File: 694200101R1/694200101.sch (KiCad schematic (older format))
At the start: 241 parts, among them J1 USB4085-GF-A, J2 Conn_01x02_Male, J3 Conn_01x02_Male, SW1 MX_SW, SW10 MX_SW, SW100 MX_SW, SW101 MX_SW, SW102 MX_SW, SW103 MX_SW, SW104 MX_SW, SW105 MX_SW, SW106 MX_SW, SW107 MX_SW, SW11 MX_SW, SW12 MX_SW, SW13 MX_SW, SW14 MX_SW, SW15 MX_SW, SW16 MX_SW, SW17 MX_SW, SW18 MX_SW, SW19 MX_SW, SW2 MX_SW, SW20 MX_SW, SW21 MX_SW, SW22 MX_SW, SW23 MX_SW, SW24 MX_SW, SW25 MX_SW, SW26 MX_SW, SW27 MX_SW, SW28 MX_SW, SW29 MX_SW, SW3 MX_SW, SW30 MX_SW, SW31 MX_SW, SW32 MX_SW, SW33 MX_SW, SW34 MX_SW, SW35 MX_SW, SW36 MX_SW, SW37 MX_SW, SW38 MX_SW, SW39 MX_SW, SW4 MX_SW, SW40 MX_SW, SW41 MX_SW, SW42 MX_SW, SW43 MX_SW, SW44 MX_SW, SW45 MX_SW, SW46 MX_SW, SW47 MX_SW, SW48 MX_SW, SW49 MX_SW, SW5 MX_SW, SW50 MX_SW, SW51 MX_SW, SW52 MX_SW, SW53 MX_SW, SW54 MX_SW, SW55 MX_SW, SW56 MX_SW, SW57 MX_SW, SW58 MX_SW, SW59 MX_SW, SW6 MX_SW, SW60 MX_SW, SW61 MX_SW, SW62 MX_SW, SW63 MX_SW, SW64 MX_SW, SW65 MX_SW, SW66 MX_SW, SW67 MX_SW, SW68 MX_SW, SW69 MX_SW, SW7 MX_SW, SW70 MX_SW, SW71 MX_SW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

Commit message: Added New Crystal to Schematic
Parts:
- removed Y1: Crystal_GND24, symbol Device:Crystal_GND24
- added Y?: ECS-480-10-33B-CKM-TR, cldg:XTAL_ECS-480-10-33B-CKM-TR, symbol cldg:ECS-480-10-33B-CKM-TR
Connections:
- wire segments 629 -> 623
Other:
- moved on the sheet: C4, C6

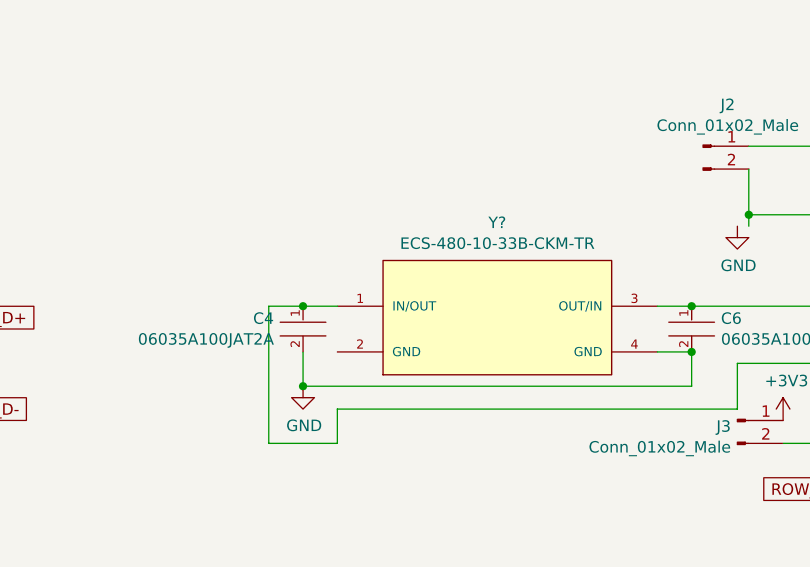
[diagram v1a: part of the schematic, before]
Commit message: LED rows 2+3
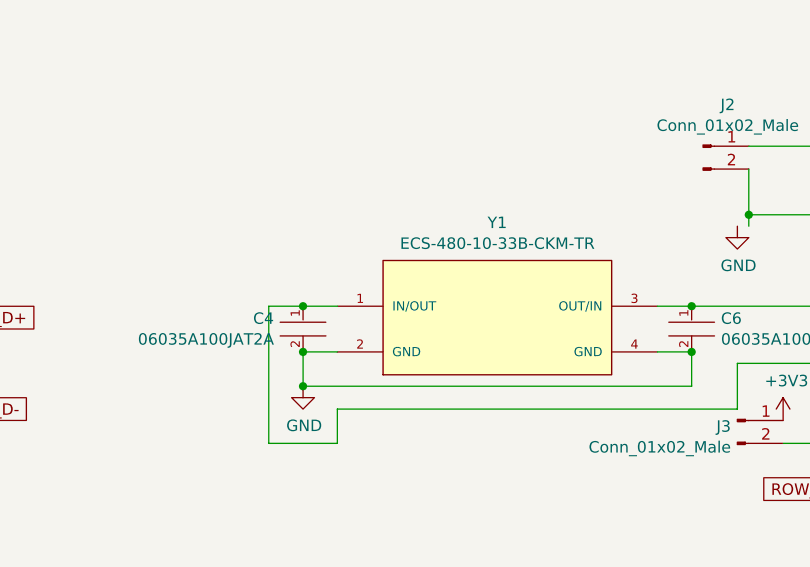
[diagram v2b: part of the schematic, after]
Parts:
- gave numbers to parts that had none: 1
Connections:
- net GND: now also Y1.2 (GND)
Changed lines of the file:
@@
 	7150 7500 7300 7500
 $Comp
-L cldg:ECS-480-10-33B-CKM-TR Y?
+L cldg:ECS-480-10-33B-CKM-TR Y1
 U 1 1 5FF4EA01
 P 6450 7400
-F 0 "Y?" H 6450 7865 50  0000 C CNN
+F 0 "Y1" H 6450 7865 50  0000 C CNN
 F 1 "ECS-480-10-33B-CKM-TR" H 6450 7774 50  0000 C CNN
 F 2 "cldg:XTAL_ECS-480-10-33B-CKM-TR" H 6150 7750 50  0001 L BNN
@@
 	7900 7300 7300 7300
 Connection ~ 7300 7300
+Wire Wire Line
+	5750 7500 5600 7500
+Connection ~ 5600 7500
 $EndSCHEMATC

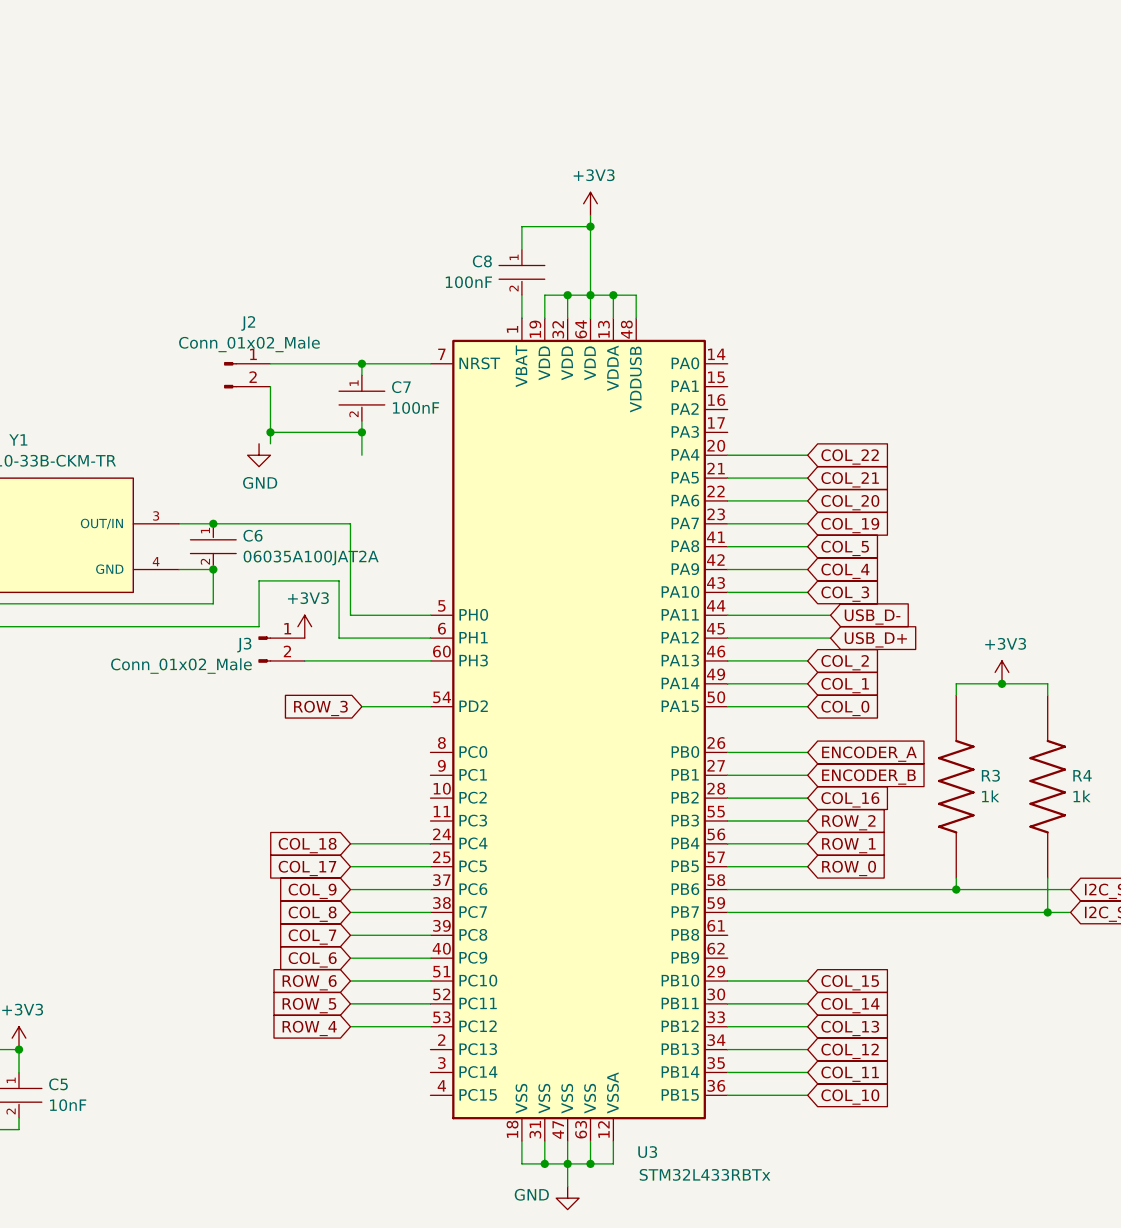
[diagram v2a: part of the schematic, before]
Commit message: Added Debug Header for Nucleo
Added debug headers for ST-V2-1 Nucleo board for advanced debugging
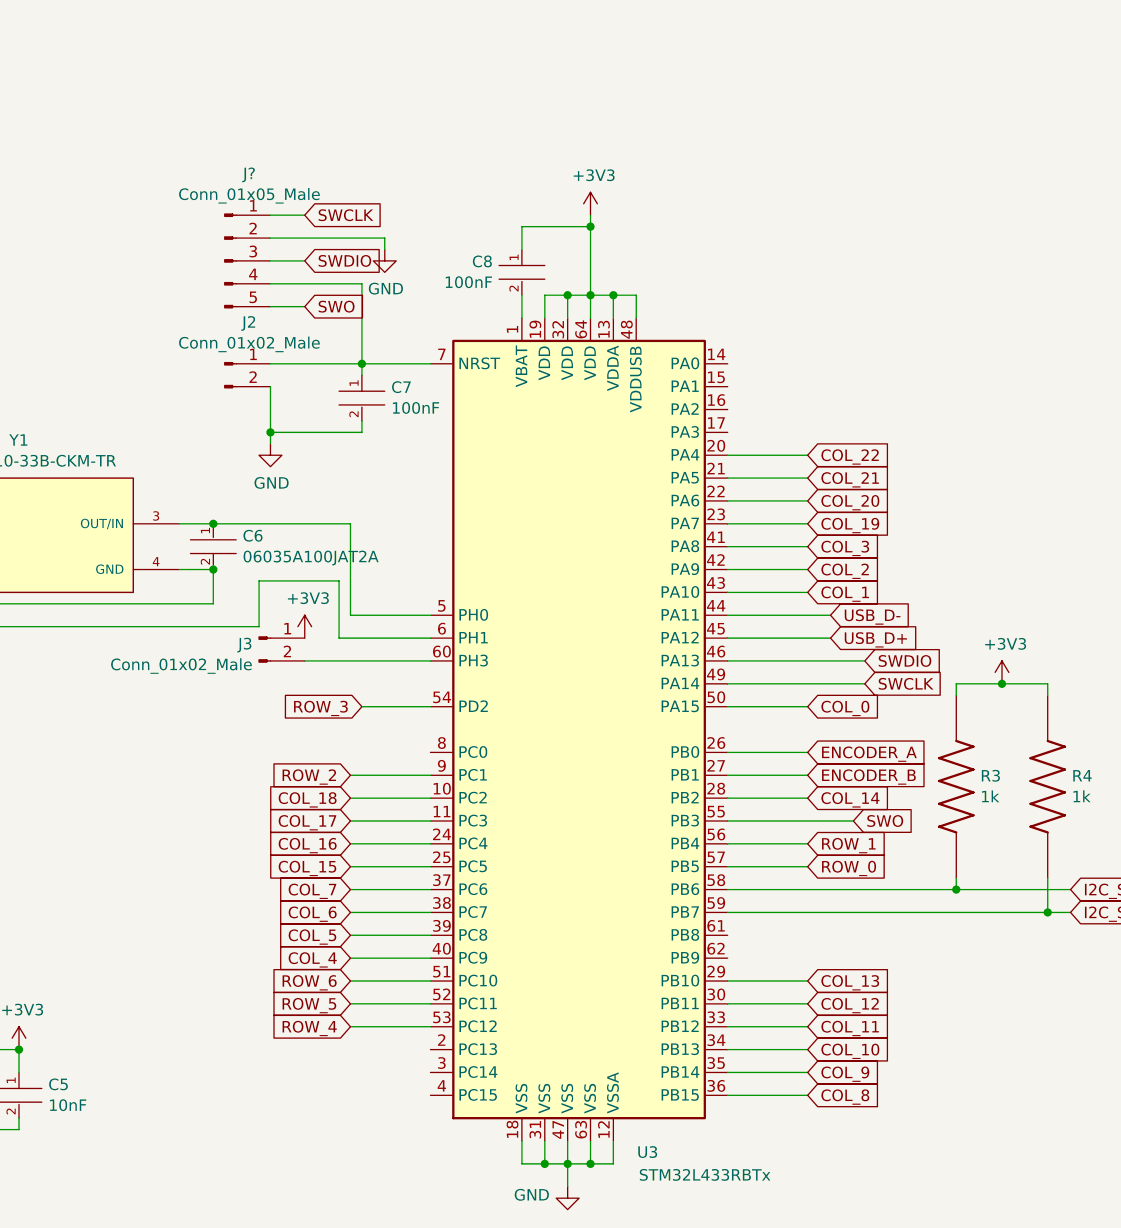
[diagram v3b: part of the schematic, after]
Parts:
- added J?: Conn_01x05_Male, Connector_PinHeader_2.54mm:PinHeader_1x05_P2.54mm_Vertical, symbol Connector:Conn_01x05_Male
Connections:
- net COL_1: now also U3.43 (PA10); no longer U3.49 (PA14)
- net COL_10: now also U3.34 (PB13); no longer U3.36 (PB15)
- net COL_11: now also U3.33 (PB12); no longer U3.35 (PB14)
- net COL_12: now also U3.30 (PB11); no longer U3.34 (PB13)
- net COL_13: now also U3.29 (PB10); no longer U3.33 (PB12)
- net COL_14: now also U3.28 (PB2); no longer U3.30 (PB11)
- net COL_15: now also U3.25 (PC5); no longer U3.29 (PB10)
- net COL_16: now also U3.24 (PC4); no longer U3.28 (PB2)
- net COL_17: now also U3.11 (PC3); no longer U3.25 (PC5)
- net COL_18: now also U3.10 (PC2); no longer U3.24 (PC4)
- net COL_2: now also U3.42 (PA9); no longer U3.46 (PA13)
- net COL_3: now also U3.41 (PA8); no longer U3.43 (PA10)
- net COL_4: now also U3.40 (PC9); no longer U3.42 (PA9)
- net COL_5: now also U3.39 (PC8); no longer U3.41 (PA8)
- net COL_6: now also U3.38 (PC7); no longer U3.40 (PC9)
- net COL_7: now also U3.37 (PC6); no longer U3.39 (PC8)
- net COL_8: now also U3.36 (PB15); no longer U3.38 (PC7)
- net COL_9: now also U3.35 (PB14); no longer U3.37 (PC6)
- net GND: now also C7.2, J2.2 (Pin_2), J?.2 (Pin_2)
- net ROW_2: now also U3.9 (PC1); no longer U3.55 (PB3)
- net at C7.1, J2.1 (Pin_1), U3.7 (NRST): now also J?.4 (Pin_4)
- new net SWCLK: J?.1 (Pin_1), U3.49 (PA14)
- new net SWDIO: J?.3 (Pin_3), U3.46 (PA13)
- new net SWO: J?.5 (Pin_5), U3.55 (PB3)
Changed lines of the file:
@@
 L power:GND #PWR09
 U 1 1 6007927B
-P 7500 6950
-F 0 "#PWR09" H 7500 6700 50  0001 C CNN
-F 1 "GND" H 7505 6777 50  0000 C CNN
-F 2 "" H 7500 6950 50  0001 C CNN
-F 3 "" H 7500 6950 50  0001 C CNN
-	1    7500 6950
+P 7550 6950
+F 0 "#PWR09" H 7550 6700 50  0001 C CNN
+F 1 "GND" H 7555 6777 50  0000 C CNN
+F 2 "" H 7550 6950 50  0001 C CNN
+F 3 "" H 7550 6950 50  0001 C CNN
+	1    7550 6950
 	1    0    0    -1
 $EndComp
@@
 Text GLabel 9900 8700 2    50   Input ~ 0
 ROW_1
-Text GLabel 9900 8600 2    50   Input ~ 0
+Text GLabel 7900 8400 0    50   Input ~ 0
 ROW_2
 Wire Wire Line
@@
 Text GLabel 9900 8100 2    50   Input ~ 0
 COL_0
-Text GLabel 9900 8000 2    50   Input ~ 0
+Text GLabel 9900 7600 2    50   Input ~ 0
 COL_1
-Text GLabel 9900 7900 2    50   Input ~ 0
+Text GLabel 9900 7500 2    50   Input ~ 0
 COL_2
-Text GLabel 9900 7600 2    50   Input ~ 0
+Text GLabel 9900 7400 2    50   Input ~ 0
 COL_3
-Text GLabel 9900 7500 2    50   Input ~ 0
+Text GLabel 7900 9200 0    50   Input ~ 0
 COL_4
-Text GLabel 9900 7400 2    50   Input ~ 0
+Text GLabel 7900 9100 0    50   Input ~ 0
 COL_5
 Wire Wire Line
 	8250 9200 7900 9200
-Text GLabel 7900 9200 0    50   Input ~ 0
+Text GLabel 7900 9000 0    50   Input ~ 0
 COL_6
 Wire Wire Line
 	8250 9100 7900 9100
-Text GLabel 7900 9100 0    50   Input ~ 0
+Text GLabel 7900 8900 0    50   Input ~ 0
 COL_7
 Wire Wire Line
 	8250 9000 7900 9000
-Text GLabel 7900 9000 0    50   Input ~ 0
+Text GLabel 9900 9800 2    50   Input ~ 0
 COL_8
 Wire Wire Line
 	8250 8900 7900 8900
-Text GLabel 7900 8900 0    50   Input ~ 0
+Text GLabel 9900 9700 2    50   Input ~ 0
 COL_9
-Text GLabel 9900 9800 2    50   Input ~ 0
+Text GLabel 9900 9600 2    50   Input ~ 0
 COL_10
-Text GLabel 9900 9700 2    50   Input ~ 0
+Text GLabel 9900 9500 2    50   Input ~ 0
 COL_11
-Text GLabel 9900 9600 2    50   Input ~ 0
+Text GLabel 9900 9400 2    50   Input ~ 0
 COL_12
-Text GLabel 9900 9500 2    50   Input ~ 0
+Text GLabel 9900 9300 2    50   Input ~ 0
 COL_13
-Text GLabel 9900 9400 2    50   Input ~ 0
+Text GLabel 9900 8500 2    50   Input ~ 0
 COL_14
-Text GLabel 9900 9300 2    50   Input ~ 0
+Text GLabel 7900 8800 0    50   Input ~ 0
 COL_15
-Text GLabel 9900 8500 2    50   Input ~ 0
+Text GLabel 7900 8700 0    50   Input ~ 0
 COL_16
 Wire Wire Line
 	8250 8800 7900 8800
-Text GLabel 7900 8800 0    50   Input ~ 0
+Text GLabel 7900 8600 0    50   Input ~ 0
 COL_17
 Wire Wire Line
 	8250 8700 7900 8700
-Text GLabel 7900 8700 0    50   Input ~ 0
+Text GLabel 7900 8500 0    50   Input ~ 0
 COL_18
 Text GLabel 9900 7300 2    50   Input ~ 0
@@
 	9550 8700 9900 8700
 Wire Wire Line
-	9550 8600 9900 8600
-Wire Wire Line
 	9550 8500 9900 8500
 Wire Wire Line
@@
 	9550 8100 9900 8100
 Wire Wire Line
-	9550 8000 9900 8000
+	9550 8000 10150 8000
 Wire Wire Line
-	9550 7900 9900 7900
+	9550 7900 10150 7900
 Wire Wire Line
 	10000 7800 9550 7800
@@
 Wire Wire Line
 	9550 7600 9900 7600
-Wire Wire Line
-	7950 7000 7950 6900
-Connection ~ 7950 6900
 $Comp
 L MCU_ST_STM32L4:STM32L433RBTx U3
@@
 	5750 7500 5600 7500
 Connection ~ 5600 7500
+Wire Wire Line
+	8250 8600 7900 8600
+Wire Wire Line
+	8250 8500 7900 8500
+Text GLabel 10150 7900 2    50   Input ~ 0
+SWDIO
+Text GLabel 10150 8000 2    50   Input ~ 0
+SWCLK
+$Comp
+L Connector:Conn_01x05_Male J?
+U 1 1 600F5E13
+P 7350 6150
+F 0 "J?" H 7458 6531 50  0000 C CNN
+F 1 "Conn_01x05_Male" H 7458 6440 50  0000 C CNN
+F 2 "Connector_PinHeader_2.54mm:PinHeader_1x05_P2.54mm_Vertical" H 7350 6150 50  0001 C CNN
+F 3 "~" H 7350 6150 50  0001 C CNN
+	1    7350 6150
+	1    0    0    -1
+$EndComp
+Wire Wire Line
+	8250 8400 7900 8400
+Text GLabel 10100 8600 2    50   Input ~ 0
+SWO
+Wire Wire Line
+	9550 8600 10100 8600
+Wire Wire Line
+	7550 5950 7700 5950
+Text GLabel 7700 5950 2    50   Input ~ 0
+SWCLK
+Wire Wire Line
+	7550 6050 8050 6050
+Wire Wire Line
+	8050 6050 8050 6100
+$Comp
+L power:GND #PWR?
+U 1 1 602A2E5A
+P 8050 6100
+F 0 "#PWR?" H 8050 5850 50  0001 C CNN
+F 1 "GND" H 8055 5927 50  0000 C CNN
+F 2 "" H 8050 6100 50  0001 C CNN
+F 3 "" H 8050 6100 50  0001 C CNN
+	1    8050 6100
+	1    0    0    -1
+$EndComp
+Wire Wire Line
+	7550 6150 7700 6150
+Text GLabel 7700 6150 2    50   Input ~ 0
+SWDIO
+Wire Wire Line
+	7950 6600 7950 6250
+Wire Wire Line
+	7950 6250 7550 6250
+Wire Wire Line
+	7550 6350 7700 6350
+Text GLabel 7700 6350 2    50   Input ~ 0
+SWO
 $EndSCHEMATC

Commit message: updated j2
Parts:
- removed J2: Conn_01x02_Male, Connector_PinHeader_2.54mm:PinHeader_1x02_P2.54mm_Vertical, symbol Connector:Conn_01x02_Male
- gave numbers to parts that had none: 1
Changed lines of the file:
@@
 	8850 10100 8850 10200
 $Comp
-L Connector:Conn_01x02_Male J2
-U 1 1 6006794B
-P 7350 6600
-F 0 "J2" H 7458 6781 50  0000 C CNN
-F 1 "Conn_01x02_Male" H 7458 6690 50  0000 C CNN
-F 2 "Connector_PinHeader_2.54mm:PinHeader_1x02_P2.54mm_Vertical" H 7350 6600 50  0001 C CNN
-F 3 "~" H 7350 6600 50  0001 C CNN
-	1    7350 6600
-	1    0    0    -1
-$EndComp
-$Comp
 L Connector:Conn_01x02_Male J3
 U 1 1 6006B89E
@@
 L power:GND #PWR09
 U 1 1 6007927B
-P 7550 6950
-F 0 "#PWR09" H 7550 6700 50  0001 C CNN
-F 1 "GND" H 7555 6777 50  0000 C CNN
-F 2 "" H 7550 6950 50  0001 C CNN
-F 3 "" H 7550 6950 50  0001 C CNN
-	1    7550 6950
+P 7950 6950
+F 0 "#PWR09" H 7950 6700 50  0001 C CNN
+F 1 "GND" H 7955 6777 50  0000 C CNN
+F 2 "" H 7950 6950 50  0001 C CNN
+F 3 "" H 7950 6950 50  0001 C CNN
+	1    7950 6950
 	1    0    0    -1
 $EndComp
@@
 	7950 6600 7950 6650
 Connection ~ 7950 6600
-Wire Wire Line
-	7950 6600 7550 6600
-Wire Wire Line
-	7950 6900 7950 6850
-Wire Wire Line
-	7550 6700 7550 6900
-Wire Wire Line
-	7550 6900 7950 6900
-Wire Wire Line
-	7550 6900 7550 6950
-Connection ~ 7550 6900
 $Comp
 L cldg:MX_SW SW1
@@
 SWCLK
 $Comp
-L Connector:Conn_01x05_Male J?
+L Connector:Conn_01x05_Male J2
 U 1 1 600F5E13
 P 7350 6150
-F 0 "J?" H 7458 6531 50  0000 C CNN
+F 0 "J2" H 7458 6531 50  0000 C CNN
 F 1 "Conn_01x05_Male" H 7458 6440 50  0000 C CNN
 F 2 "Connector_PinHeader_2.54mm:PinHeader_1x05_P2.54mm_Vertical" H 7350 6150 50  0001 C CNN
@@
 Text GLabel 7700 6350 2    50   Input ~ 0
 SWO
+Wire Wire Line
+	7950 6850 7950 6950
 $EndSCHEMATC

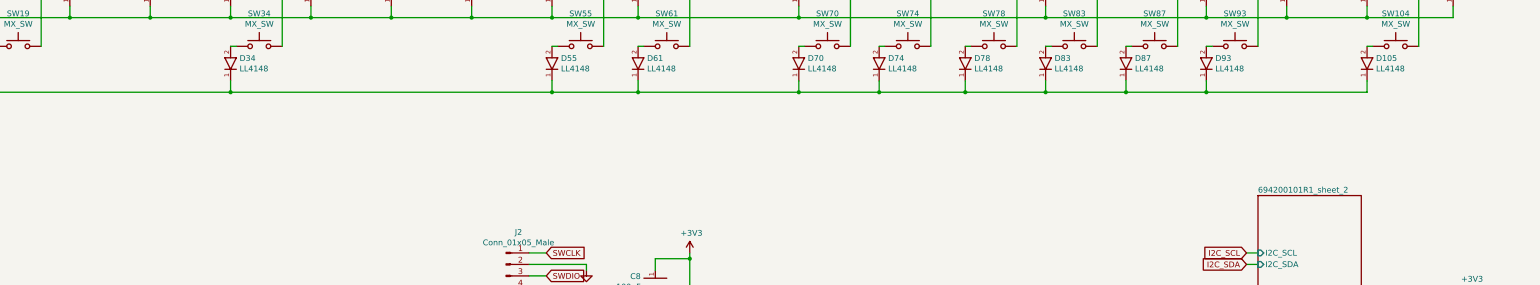
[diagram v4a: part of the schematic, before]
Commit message: Added Stabs as Components
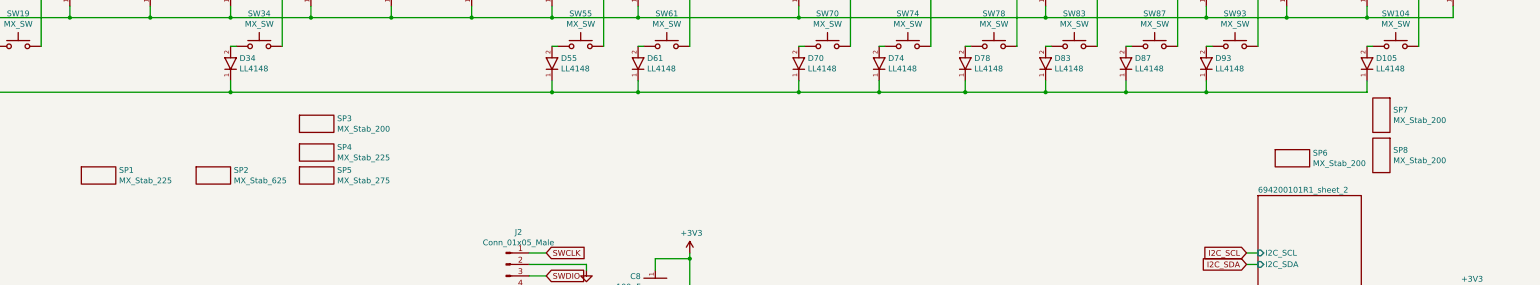
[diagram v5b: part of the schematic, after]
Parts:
- added SP1, SP4: MX_Stab_225, keyboard_parts:Mx_Stab_225, symbol cldg:MX_Stab_225
- added SP2: MX_Stab_625, keyboard_parts:Mx_Stab_625, symbol cldg:MX_Stab_625
- added SP3, SP6, SP7, SP8: MX_Stab_200, keyboard_parts:Mx_Stab_200, symbol cldg:MX_Stab_200
- added SP5: MX_Stab_275, keyboard_parts:Mx_Stab_275, symbol cldg:MX_Stab_275
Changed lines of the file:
@@
 	8050 6050 8050 6100
 $Comp
-L power:GND #PWR?
+L power:GND #PWR0101
 U 1 1 602A2E5A
 P 8050 6100
-F 0 "#PWR?" H 8050 5850 50  0001 C CNN
+F 0 "#PWR0101" H 8050 5850 50  0001 C CNN
 F 1 "GND" H 8055 5927 50  0000 C CNN
 F 2 "" H 8050 6100 50  0001 C CNN
@@
 Wire Wire Line
 	7950 6850 7950 6950
+$Comp
+L cldg:MX_Stab_225 SP1
+U 1 1 60679C49
+P 3800 5400
+F 0 "SP1" H 3978 5571 50  0000 L CNN
+F 1 "MX_Stab_225" H 3978 5480 50  0000 L CNN
+F 2 "keyboard_parts:Mx_Stab_225" H 4100 5300 50  0001 C CNN
+F 3 "" H 3800 5400 50  0001 C CNN
+	1    3800 5400
+	1    0    0    -1
+$EndComp
+$Comp
+L cldg:MX_Stab_625 SP2
+U 1 1 6067B387
+P 4800 5400
+F 0 "SP2" H 4978 5571 50  0000 L CNN
+F 1 "MX_Stab_625" H 4978 5480 50  0000 L CNN
+F 2 "keyboard_parts:Mx_Stab_625" H 5100 5300 50  0001 C CNN
+F 3 "" H 4800 5400 50  0001 C CNN
+	1    4800 5400
+	1    0    0    -1
+$EndComp
+$Comp
+L cldg:MX_Stab_275 SP5
+U 1 1 60680784
+P 5700 5400
+F 0 "SP5" H 5878 5571 50  0000 L CNN
+F 1 "MX_Stab_275" H 5878 5480 50  0000 L CNN
+F 2 "keyboard_parts:Mx_Stab_275" H 6000 5300 50  0001 C CNN
+F 3 "" H 5700 5400 50  0001 C CNN
+	1    5700 5400
+	1    0    0    -1
+$EndComp
+$Comp
+L cldg:MX_Stab_225 SP4
+U 1 1 606E9194
+P 5700 5200
+F 0 "SP4" H 5878 5371 50  0000 L CNN
+F 1 "MX_Stab_225" H 5878 5280 50  0000 L CNN
+F 2 "keyboard_parts:Mx_Stab_225" H 6000 5100 50  0001 C CNN
+F 3 "" H 5700 5200 50  0001 C CNN
+	1    5700 5200
+	1    0    0    -1
+$EndComp
+$Comp
+L cldg:MX_Stab_200 SP3
+U 1 1 606EC67F
+P 5700 4950
+F 0 "SP3" H 5878 5121 50  0000 L CNN
+F 1 "MX_Stab_200" H 5878 5030 50  0000 L CNN
+F 2 "keyboard_parts:Mx_Stab_200" H 6000 4850 50  0001 C CNN
+F 3 "" H 5700 4950 50  0001 C CNN
+	1    5700 4950
+	1    0    0    -1
+$EndComp
+$Comp
+L cldg:MX_Stab_200 SP6
+U 1 1 606EDF78
+P 14200 5250
+F 0 "SP6" H 14378 5421 50  0000 L CNN
+F 1 "MX_Stab_200" H 14378 5330 50  0000 L CNN
+F 2 "keyboard_parts:Mx_Stab_200" H 14500 5150 50  0001 C CNN
+F 3 "" H 14200 5250 50  0001 C CNN
+	1    14200 5250
+	1    0    0    -1
+$EndComp
+$Comp
+L cldg:MX_Stab_200 SP8
+U 1 1 606EEEFE
+P 14850 5100
+F 0 "SP8" V 14804 5328 50  0000 L CNN
+F 1 "MX_Stab_200" V 14895 5328 50  0000 L CNN
+F 2 "keyboard_parts:Mx_Stab_200" H 15150 5000 50  0001 C CNN
+F 3 "" H 14850 5100 50  0001 C CNN
+	1    14850 5100
+	0    1    1    0
+$EndComp
+$Comp
+L cldg:MX_Stab_200 SP7
+U 1 1 606F1E94
+P 14850 4750
+F 0 "SP7" V 14804 4978 50  0000 L CNN
+F 1 "MX_Stab_200" V 14895 4978 50  0000 L CNN
+F 2 "keyboard_parts:Mx_Stab_200" H 15150 4650 50  0001 C CNN
+F 3 "" H 14850 4750 50  0001 C CNN
+	1    14850 4750
+	0    1    1    0
+$EndComp
 $EndSCHEMATC
